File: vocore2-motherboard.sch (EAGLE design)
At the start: 92 parts, among them IC1 AP63205, IC2 FE1.1S, IC3 LM3671MF-3.3, IC4 LM3671MF-3.3, IC5 LM3671MF-3.3, IC6 FT232R, IC7 SN74LVC2G14DBVR, J1 RJHSE-5381, J2 TE_1775470-8, J3 AMPHENOL_1140084168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

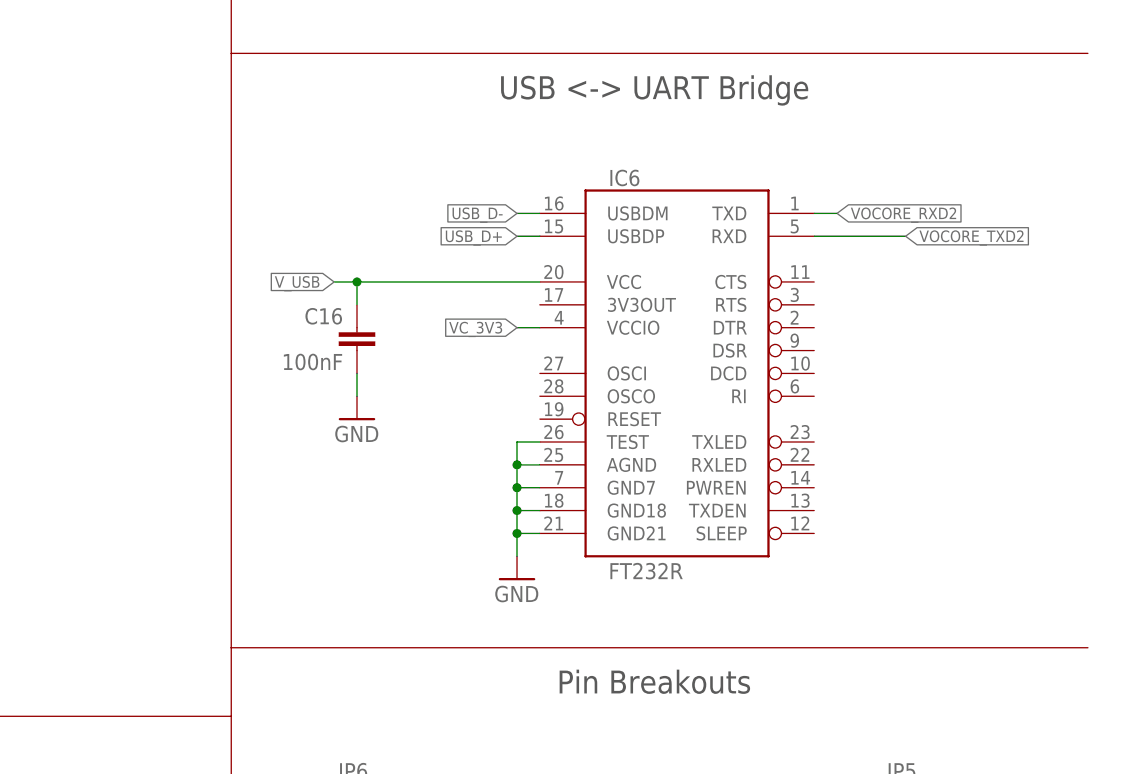
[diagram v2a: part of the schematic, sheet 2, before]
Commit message: feat: use FT230X instead of FT232R
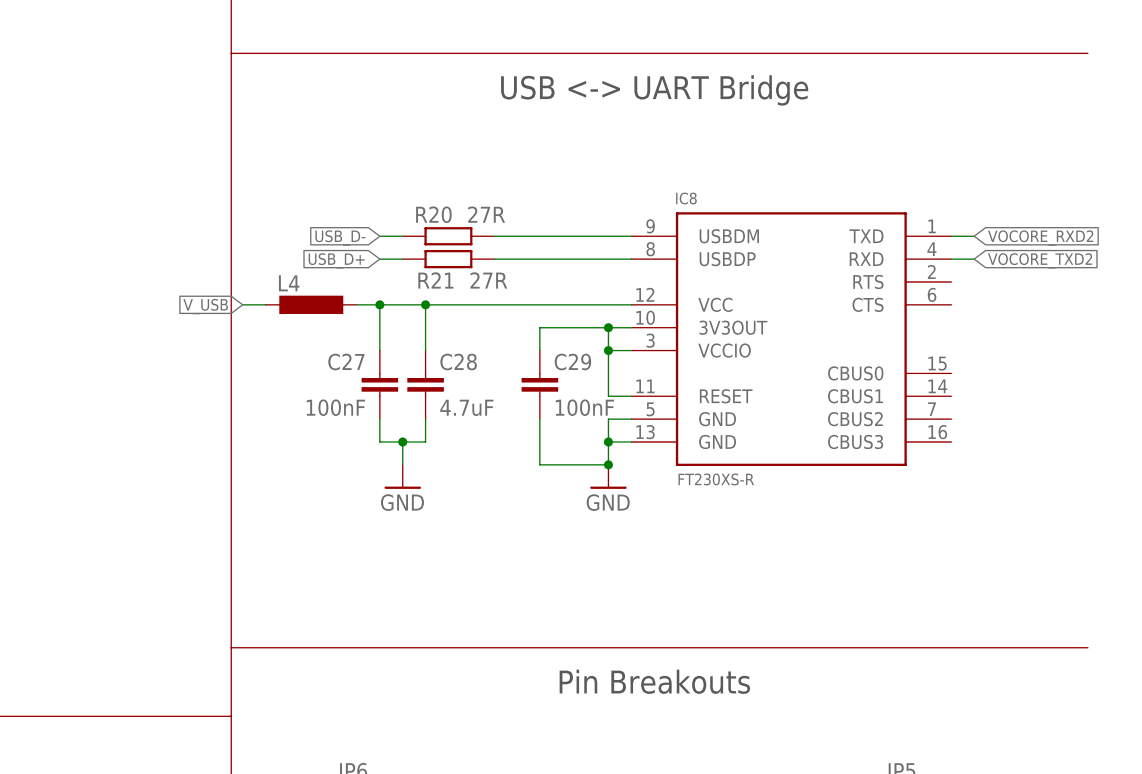
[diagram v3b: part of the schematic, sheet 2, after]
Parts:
- removed C16: 100nF, rcl:C-EUC0603
- removed IC6: FT232R, SparkFun:FT232RLSSOP
- added C27, C29: 100nF, rcl:C-EUC0603
- added C28: 4.7uF, rcl:C-EUC0603
- added IC8: FT230XS-R, ftdi:FT230XS-R
- added L4: (no value), rcl:L-EUL0805
- added R20, R21: 27R, rcl:R-EU_R0603
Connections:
- new net FT230_VCCIO: C29.1, IC8.3V3OUT, IC8.RESET, IC8.VCCIO
- new net N$35: C27.1, C28.1, IC8.VCC, L4.1
- new net N$36: IC8.USBDM, R20.2
- new net N$38: IC8.USBDP, R21.1
- net GND: now also C27.2, C28.2, C29.2, IC8.GND, IC8.GND@1; no longer C16.2, IC6.AGND, IC6.GND18, IC6.GND21, IC6.GND7, IC6.TEST
- net USB_D+: now also R21.2; no longer IC6.USBDP
- net USB_D-: now also R20.1; no longer IC6.USBDM
- net VC_3V3: no longer IC6.VCCIO
- net VOCORE_RXD2: now also IC8.TXD; no longer IC6.TXD
- net VOCORE_TXD2: now also IC8.RXD; no longer IC6.RXD
- net V_USB: now also L4.2; no longer C16.1, IC6.VCC

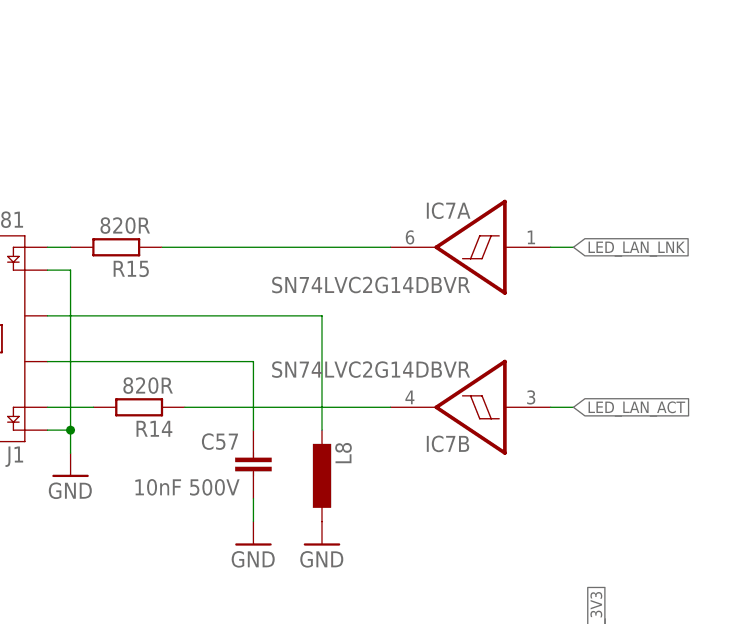
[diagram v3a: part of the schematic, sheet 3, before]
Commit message: feat(pcb): mounting hole for vocore
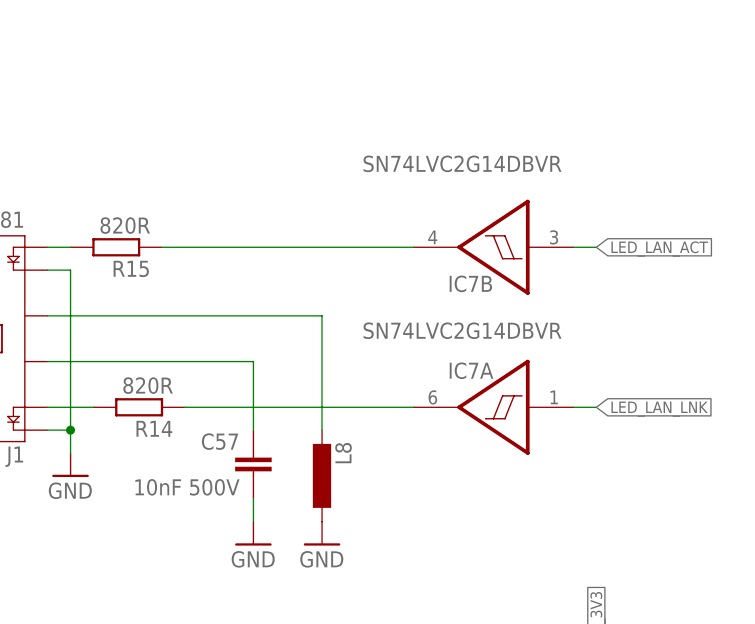
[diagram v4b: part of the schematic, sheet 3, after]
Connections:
- removed net N$46: U1.GPIO42
- removed net N$67: IC7B.O, R14.1
- new net N$35165: U1.GPIO38
- new net N$37: IC7B.O, R15.1
- net LED_LAN_LNK: now also U1.GPIO42; no longer U1.GPIO38
- net N$66: now also R14.1; no longer R15.1
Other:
- moved on the sheet: IC7A, IC7B
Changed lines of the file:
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@@
 <net name="LED_LAN_LNK" class="0">
 <segment>
-<pinref part="U1" gate="G$1" pin="GPIO38"/>
-<wire x1="116.84" y1="91.44" x2="119.38" y2="91.44" width="0.1524" layer="91"/>
-<label x="119.38" y="91.44" size="1.27" layer="95" xref="yes"/>
+<pinref part="U1" gate="G$1" pin="GPIO42"/>
+<wire x1="116.84" y1="81.28" x2="121.92" y2="81.28" width="0.1524" layer="91"/>
+<label x="121.92" y="81.28" size="1.27" layer="95" xref="yes"/>
 </segment>
 </net>
@@
 <pinref part="U1" gate="G$1" pin="GPIO41"/>
 <wire x1="116.84" y1="83.82" x2="119.38" y2="83.82" width="0.1524" layer="91"/>
-</segment>
-</net>
-<net name="N$46" class="0">
-<segment>
-<pinref part="U1" gate="G$1" pin="GPIO42"/>
-<wire x1="116.84" y1="81.28" x2="119.38" y2="81.28" width="0.1524" layer="91"/>
 </segment>
 </net>
@@
 </segment>
 </net>
+<net name="N$35165" class="0">
+<segment>
+<pinref part="U1" gate="G$1" pin="GPIO38"/>
+<wire x1="116.84" y1="91.44" x2="119.38" y2="91.44" width="0.1524" layer="91"/>
+</segment>
+</net>
 </nets>
 </sheet>
@@
 <attribute name="DIGIKEY" x="180.34" y="106.68" size="1.778" layer="96" rot="R180" display="off"/>
 </instance>
-<instance part="IC7" gate="A" x="220.98" y="106.68" smashed="yes" rot="MR0">
-<attribute name="NAME" x="219.71" y="109.855" size="1.778" layer="95" font="vector" rot="MR0"/>
-<attribute name="VALUE" x="219.71" y="101.6" size="1.778" layer="96" font="vector" rot="MR0"/>
-<attribute name="DIGIKEY" x="220.98" y="106.68" size="1.778" layer="96" rot="MR0" display="off"/>
-</instance>
-<instance part="IC7" gate="B" x="220.98" y="88.9" smashed="yes" rot="R180">
-<attribute name="NAME" x="219.71" y="85.725" size="1.778" layer="95" font="vector" rot="R180"/>
-<attribute name="VALUE" x="219.71" y="93.98" size="1.778" layer="96" font="vector" rot="R180"/>
+<instance part="IC7" gate="A" x="223.52" y="88.9" smashed="yes" rot="MR0">
+<attribute name="NAME" x="222.25" y="92.075" size="1.778" layer="95" font="vector" rot="MR0"/>
+<attribute name="VALUE" x="229.87" y="96.52" size="1.778" layer="96" font="vector" rot="MR0"/>
+<attribute name="DIGIKEY" x="223.52" y="88.9" size="1.778" layer="96" rot="MR0" display="off"/>
+</instance>
+<instance part="IC7" gate="B" x="223.52" y="106.68" smashed="yes" rot="R180">
+<attribute name="NAME" x="222.25" y="103.505" size="1.778" layer="95" font="vector" rot="R180"/>
+<attribute name="VALUE" x="229.87" y="116.84" size="1.778" layer="96" font="vector" rot="R180"/>
 </instance>
 <instance part="IC7" gate="C" x="233.68" y="50.8" smashed="yes">
@@
 <net name="N$66" class="0">
 <segment>
+<pinref part="R14" gate="G$1" pin="1"/>
 <pinref part="IC7" gate="A" pin="O"/>
-<pinref part="R15" gate="G$1" pin="1"/>
-<wire x1="210.82" y1="106.68" x2="185.42" y2="106.68" width="0.1524" layer="91"/>
-</segment>
-</net>
-<net name="N$67" class="0">
-<segment>
-<pinref part="IC7" gate="B" pin="O"/>
-<pinref part="R14" gate="G$1" pin="1"/>
-<wire x1="210.82" y1="88.9" x2="187.96" y2="88.9" width="0.1524" layer="91"/>
+<wire x1="187.96" y1="88.9" x2="213.36" y2="88.9" width="0.1524" layer="91"/>
 </segment>
 </net>
@@
 <segment>
 <pinref part="IC7" gate="A" pin="I"/>
-<wire x1="228.6" y1="106.68" x2="231.14" y2="106.68" width="0.1524" layer="91"/>
-<label x="231.14" y="106.68" size="1.27" layer="95" xref="yes"/>
+<wire x1="231.14" y1="88.9" x2="233.68" y2="88.9" width="0.1524" layer="91"/>
+<label x="233.68" y="88.9" size="1.27" layer="95" xref="yes"/>
 </segment>
 </net>
@@
 <segment>
 <pinref part="IC7" gate="B" pin="I"/>
-<wire x1="228.6" y1="88.9" x2="231.14" y2="88.9" width="0.1524" layer="91"/>
-<label x="231.14" y="88.9" size="1.27" layer="95" xref="yes"/>
-</segment>
-</net>
+<wire x1="231.14" y1="106.68" x2="233.68" y2="106.68" width="0.1524" layer="91"/>
+<label x="233.68" y="106.68" size="1.27" layer="95" xref="yes"/>
+</segment>
+</net>
+<net name="N$37" class="0">
+<segment>
+<pinref part="IC7" gate="B" pin="O"/>
+<wire x1="185.42" y1="106.68" x2="213.36" y2="106.68" width="0.1524" layer="91"/>
+<pinref part="R15" gate="G$1" pin="1"/>
+</segment>
+</net>

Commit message: fix(brd): proper heatsink dimensions
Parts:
- added C16: 100nF, rcl:C-EUC0603
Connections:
- net GND: now also C16.2
- net VC_3V3: now also C16.1
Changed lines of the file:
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@@
 <attribute name="PREIS" value="0,84"/>
 </part>
-<part name="D1" library="diode" deviceset="ZENER-DIODE" device="SMB" value="1SMB5935B">
+<part name="D1" library="diode" library_urn="urn:adsk.eagle:library:210" deviceset="ZENER-DIODE" device="SMB" package3d_urn="urn:adsk.eagle:package:43404/2" value="1SMB5935B">
 <attribute name="FARNELL" value="1431177"/>
 <attribute name="MBM" value="10"/>
@@
 <attribute name="PREIS" value="0,61"/>
 </part>
-<part name="D3" library="diode" deviceset="DIODE-" device="SMB">
+<part name="D3" library="diode" library_urn="urn:adsk.eagle:library:210" deviceset="DIODE-" device="SMB" package3d_urn="urn:adsk.eagle:package:43404/2">
 <attribute name="FARNELL" value="1858651"/>
 <attribute name="LCSC" value="C110478"/>
@@
 <part name="GND9" library="supply1" deviceset="GND" device=""/>
 <part name="R3" library="rcl" library_urn="urn:adsk.eagle:library:334" deviceset="R-EU_" device="R0603" package3d_urn="urn:adsk.eagle:package:23555/3" value="330R"/>
-<part name="IC4" library="texas" deviceset="LM3671" device="" value="LM3671MF-3.3">
+<part name="IC4" library="texas" library_urn="urn:adsk.eagle:library:387" deviceset="LM3671" device="" value="LM3671MF-3.3">
 <attribute name="DIGIKEY" value="LM3671MF-3.3/NOPBCT-ND"/>
 <attribute name="FARNELL" value="1685767"/>
@@
 </part>
 <part name="GND64" library="supply1" deviceset="GND" device=""/>
-<part name="L10" library="inductor-coilcraft" deviceset="DO3314" device="" value="2.2µH">
+<part name="L10" library="inductor-coilcraft" library_urn="urn:adsk.eagle:library:240" deviceset="DO3314" device="" value="2.2µH">
 <attribute name="DIGIKEY" value="445-8725-1-ND"/>
 <attribute name="FARNELL" value="2457514"/>
@@
 <part name="GND65" library="supply1" deviceset="GND" device=""/>
 <part name="FRAME4" library="frames" library_urn="urn:adsk.eagle:library:229" deviceset="A4L-LOC" device=""/>
-<part name="IC3" library="texas" deviceset="LM3671" device="" value="LM3671MF-3.3">
+<part name="IC3" library="texas" library_urn="urn:adsk.eagle:library:387" deviceset="LM3671" device="" value="LM3671MF-3.3">
 <attribute name="DIGIKEY" value="LM3671MF-3.3/NOPBCT-ND"/>
 <attribute name="FARNELL" value="1685767"/>
@@
 </part>
 <part name="GND7" library="supply1" deviceset="GND" device=""/>
-<part name="L2" library="inductor-coilcraft" deviceset="DO3314" device="" value="2.2µH">
+<part name="L2" library="inductor-coilcraft" library_urn="urn:adsk.eagle:library:240" deviceset="DO3314" device="" value="2.2µH">
 <attribute name="DIGIKEY" value="445-8725-1-ND"/>
 <attribute name="FARNELL" value="2457514"/>
 </part>
 <part name="GND14" library="supply1" deviceset="GND" device=""/>
-<part name="IC5" library="texas" deviceset="LM3671" device="" value="LM3671MF-3.3">
+<part name="IC5" library="texas" library_urn="urn:adsk.eagle:library:387" deviceset="LM3671" device="" value="LM3671MF-3.3">
 <attribute name="DIGIKEY" value="LM3671MF-3.3/NOPBCT-ND"/>
 <attribute name="FARNELL" value="1685767"/>
@@
 </part>
 <part name="GND16" library="supply1" deviceset="GND" device=""/>
-<part name="L3" library="inductor-coilcraft" deviceset="DO3314" device="" value="2.2µH">
+<part name="L3" library="inductor-coilcraft" library_urn="urn:adsk.eagle:library:240" deviceset="DO3314" device="" value="2.2µH">
 <attribute name="DIGIKEY" value="445-8725-1-ND"/>
 <attribute name="FARNELL" value="2457514"/>
@@
 <part name="GND24" library="supply1" library_urn="urn:adsk.eagle:library:371" deviceset="GND" device=""/>
 <part name="X6" library="con-usb-3" deviceset="USB" device="-MB-S"/>
-<part name="D4" library="diode" deviceset="PRTR5V0U2X" device="">
+<part name="D4" library="diode" library_urn="urn:adsk.eagle:library:210" deviceset="PRTR5V0U2X" device="">
 <attribute name="DIGIKEY" value="1727-3884-1-ND"/>
 <attribute name="FARNELL" value="1524157"/>
@@
 <part name="J1" library="RJHSE-5381" deviceset="RJHSE-5381" device=""/>
 <part name="GND32" library="supply1" deviceset="GND" device=""/>
-<part name="D2" library="diode" deviceset="DIODE-" device="SMB">
+<part name="D2" library="diode" library_urn="urn:adsk.eagle:library:210" deviceset="DIODE-" device="SMB" package3d_urn="urn:adsk.eagle:package:43404/2">
 <attribute name="FARNELL" value="1858651"/>
 <attribute name="LCSC" value="C110478"/>
@@
 <attribute name="DIGIKEY" value="A129687CT-ND"/>
 </part>
-<part name="IC7" library="74xx-little-de" deviceset="74*2G17" device="DBV" value="SN74LVC2G14DBVR">
+<part name="IC7" library="74xx-little-de" library_urn="urn:adsk.eagle:library:86" deviceset="74*2G17" device="DBV" value="SN74LVC2G14DBVR">
 <attribute name="DIGIKEY" value="296-13010-1-ND"/>
 </part>
@@
 </pinmapping>
 </spice>
+</part>
+<part name="C16" library="rcl" library_urn="urn:adsk.eagle:library:334" deviceset="C-EU" device="C0603" package3d_urn="urn:adsk.eagle:package:23616/2" value="100nF">
+<spice>
+<pinmapping spiceprefix="C">
+<pinmap gate="G$1" pin="1" pinorder="1"/>
+<pinmap gate="G$1" pin="2" pinorder="2"/>
+</pinmapping>
+</spice>
+<attribute name="DIGIKEY" value="490-4780-1-ND"/>
 </part>
 </parts>
@@
 <attribute name="VALUE" x="30.226" y="58.42" size="1.778" layer="96"/>
 </instance>
+<instance part="C16" gate="G$1" x="243.84" y="53.34" smashed="yes">
+<attribute name="NAME" x="245.364" y="53.721" size="1.778" layer="95"/>
+<attribute name="DIGIKEY" x="243.84" y="53.34" size="1.778" layer="96" display="off"/>
+</instance>
 </instances>
 <busses>
@@
 <wire x1="233.68" y1="43.18" x2="233.68" y2="40.64" width="0.1524" layer="91"/>
 <pinref part="GND40" gate="1" pin="GND"/>
+<wire x1="233.68" y1="43.18" x2="243.84" y2="43.18" width="0.1524" layer="91"/>
+<junction x="233.68" y="43.18"/>
+<pinref part="C16" gate="G$1" pin="2"/>
+<wire x1="243.84" y1="43.18" x2="243.84" y2="48.26" width="0.1524" layer="91"/>
 </segment>
 </net>
@@
 <wire x1="233.68" y1="58.42" x2="233.68" y2="60.96" width="0.1524" layer="91"/>
 <label x="233.68" y="60.96" size="1.27" layer="95" rot="R90" xref="yes"/>
-</segment>
-</net>
+<wire x1="233.68" y1="58.42" x2="243.84" y2="58.42" width="0.1524" layer="91"/>
+<junction x="233.68" y="58.42"/>
+<pinref part="C16" gate="G$1" pin="1"/>
+<wire x1="243.84" y1="58.42" x2="243.84" y2="55.88" width="0.1524" layer="91"/>
+</segment>
+</net>
